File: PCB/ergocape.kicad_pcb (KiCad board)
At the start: 2 copper layers, 183.2 x 140.8 mm, 87 parts, among them J1 AudioJack4, J2 AudioJack4, M1 >VALUE

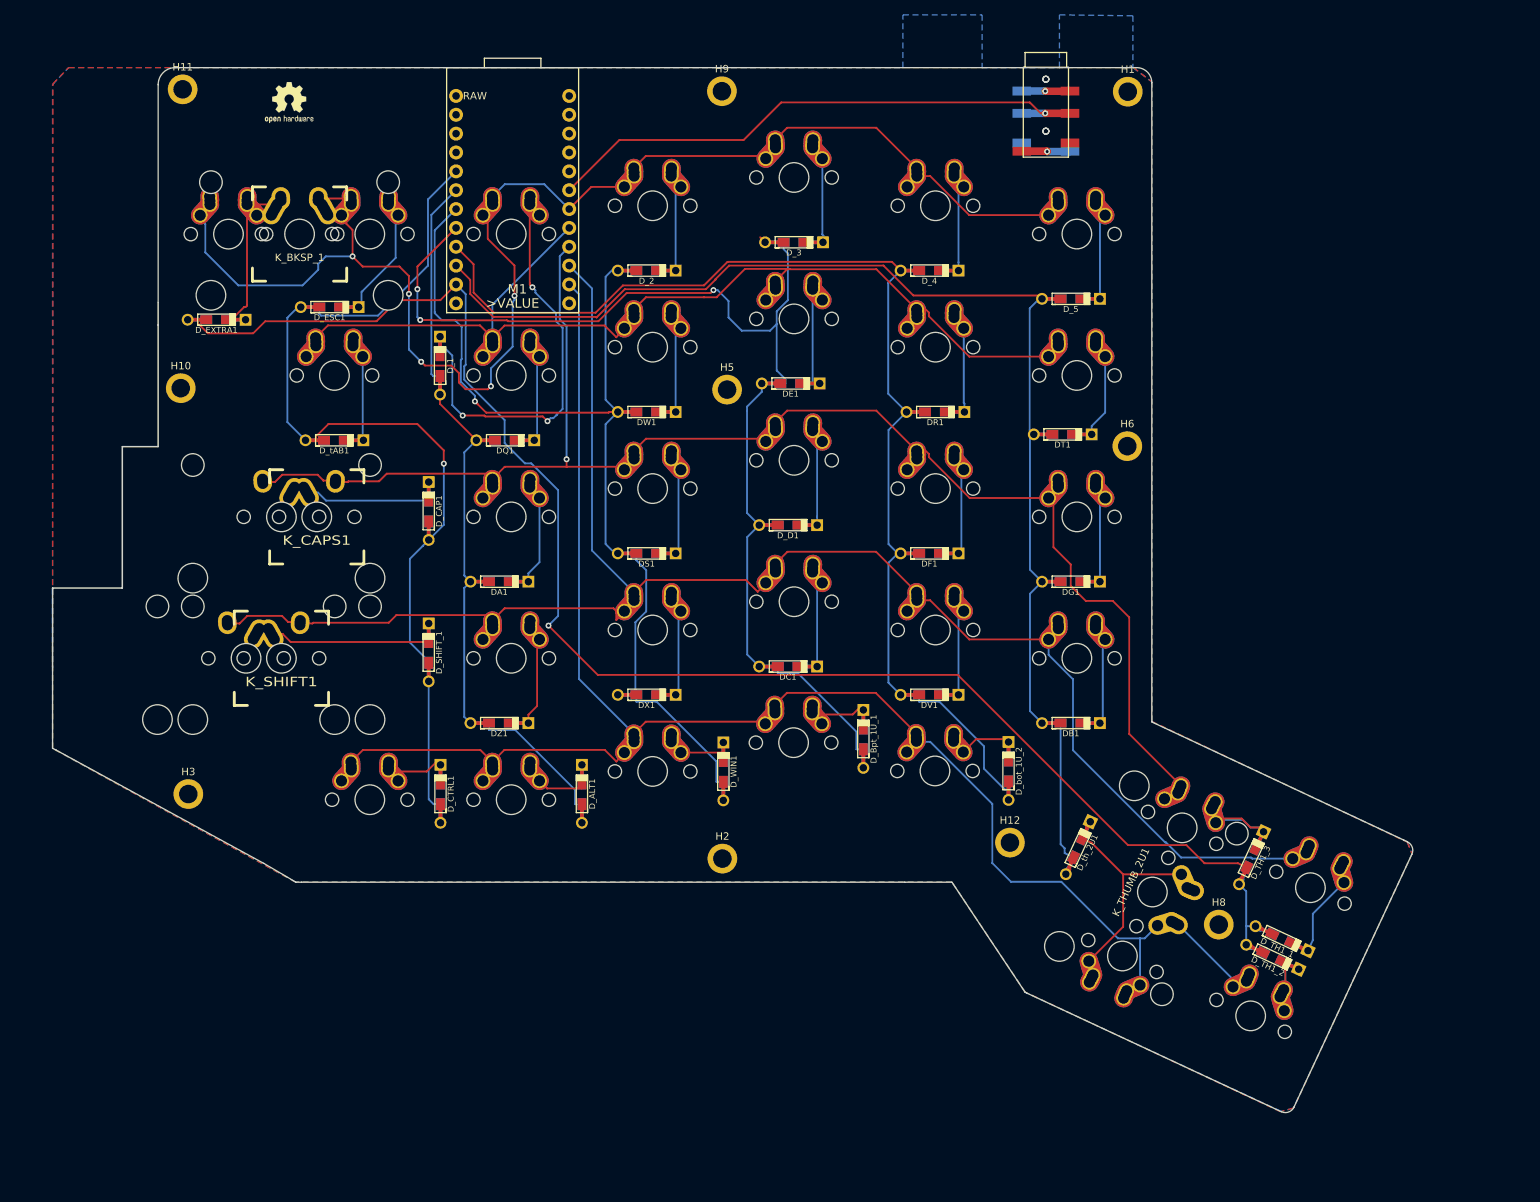
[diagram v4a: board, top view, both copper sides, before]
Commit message: finalize plate and mounting holes
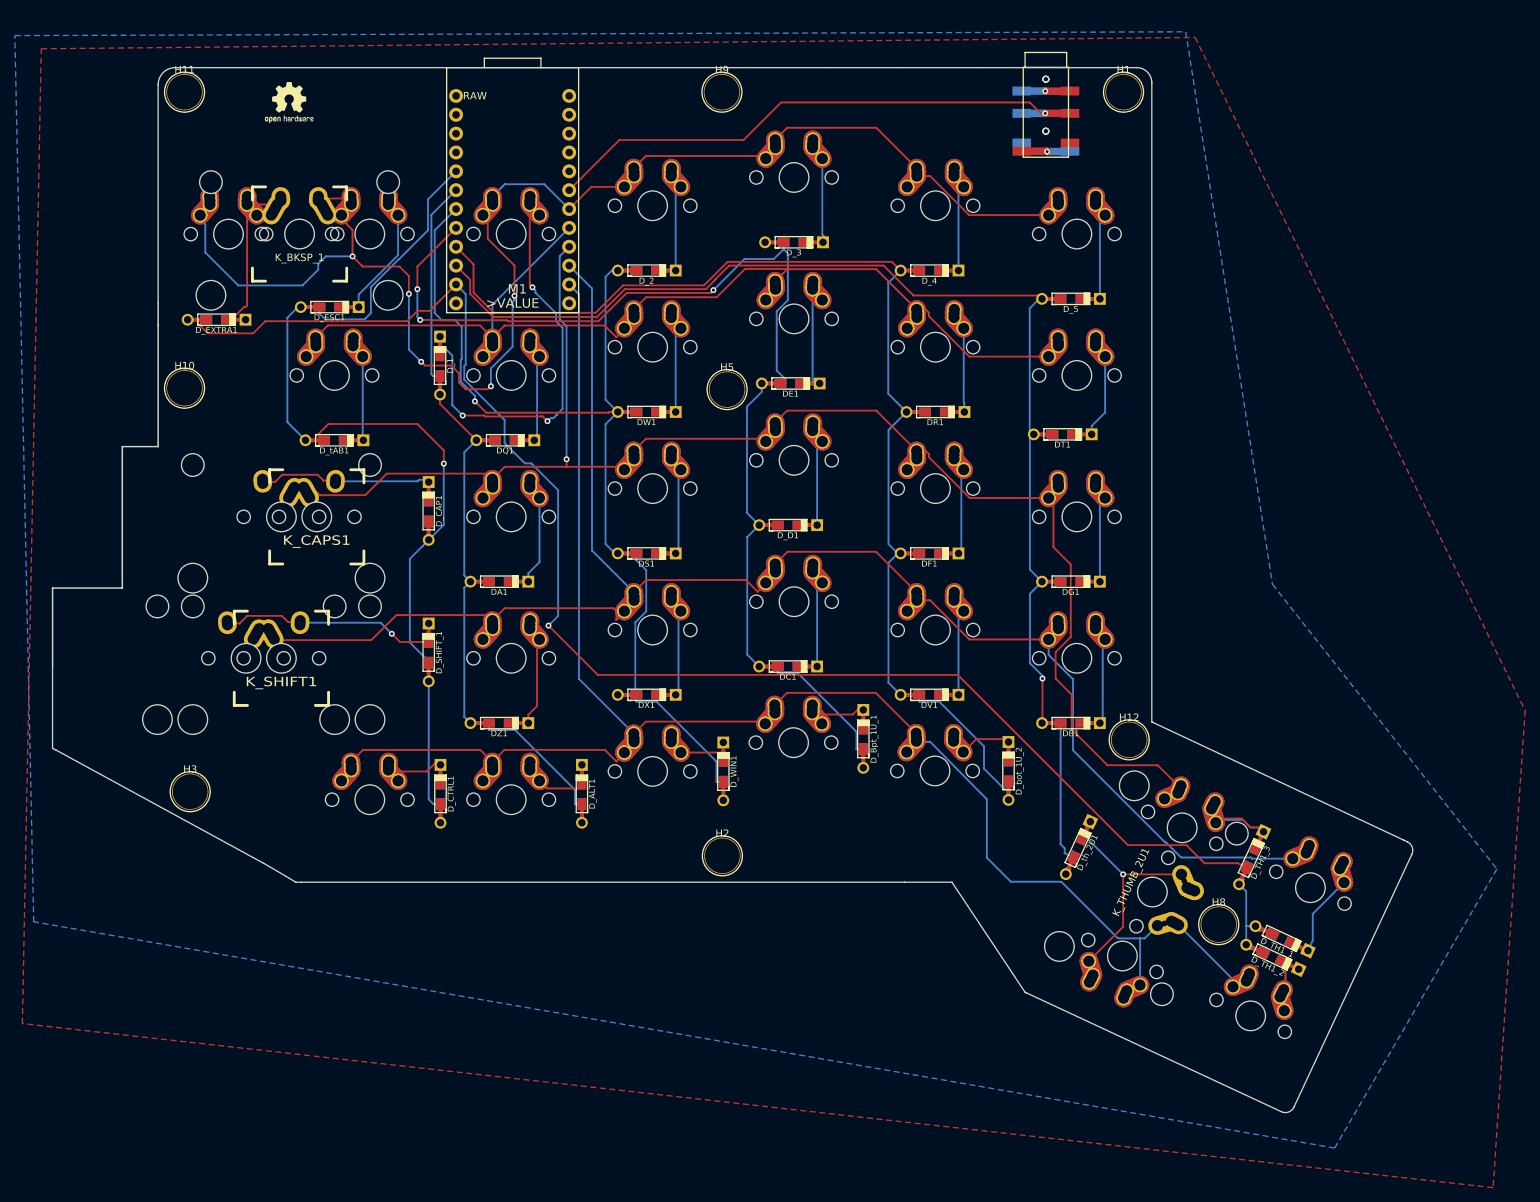
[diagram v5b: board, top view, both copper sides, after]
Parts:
- removed H6: MountingHole, acheron_MountingHoles:MountingHole_2.5x4.0mm
- H1, H10, H11, H12, H2, H3, H5, H8, H9: footprint acheron_MountingHoles:MountingHole_2.5x4.0mm -> usbc_footprint:mounting_hole_4.7x5.2mm
- moved H12 21.2 mm to (167.4, 107.8)
- moved H1 0.58 mm to (166.6, 20.6)
- moved H10 0.51 mm to (40.1, 60.5)
- moved H11 0.46 mm to (40.1, 20.6)
- moved H3 0.41 mm to (40.9, 114.8)
- moved H2 0.38 mm to (112.6, 123.4)
- moved H9 0.13 mm to (112.5, 20.6)
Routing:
- net Net-(D_CAP1-Pad1): track 22.8 -> 28.5 mm
- net Net-(D_SHIFT_1-Pad1): track 28.7 -> 34.0 mm, vias 0 -> 1
- net /ROW4: track 246.6 -> 243.3 mm
- net /COL4: track 174.7 -> 173.1 mm
- net Net-(D_th_2U1-Pad1): track 42.4 -> 42.9 mm, vias 0 -> 1
- net /COL6: track 192.7 -> 192.8 mm, vias 0 -> 1
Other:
- outline, holes or cut-outs redrawn
